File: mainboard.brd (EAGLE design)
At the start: 90.2 x 95.9 mm, 8 parts, among them IC1 FT232RLSSOP, U1 ATMEGA2560AU, U2 ITG-3200

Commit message: Initial commit of power board
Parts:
- removed IC1: FT232RLSSOP, SparkFun:SSOP28DB
- removed U$1: RFM23BP, RFM23BP:RFM23BP
- added C1, C10, C2, C3, C5, C6, C7, C8, C9: 0.1uF, SparkFun:0603-CAP
- added C4: 0.1uF, SparkFun:0402-CAP
- added JP1, JP2: USB-SMD-NS, SparkFun-Connectors:USB-MINIB-NOSTOP
- added LED2: yellow, SparkFun:LED-0603
- added R1, R4, R5: 10k, SparkFun:0603-RES
- added R3: 10k, SparkFun:0402-RES
- added R7: 470, SparkFun:0402-RES
- added SMA1: BU-SMA-V, con-coax:BU-SMA-V
- added U5: ITG-3200, SparkFun-Sensors:QFN-24
- added U6: (no value), SparkFun-DigitalIC:TSSOP14
- added U7: ATMEGA328P, SparkFun:TQFP32-08
- added U8: FT232RLSSOP, SparkFun:SSOP28DB
- added Y1: RESONATORSMD, SparkFun:RESONATOR-SMD
- added Y2: 16MHZ, SparkFun-FreqCtrl:RESONATOR-SMD
- U1: device SparkFun-DigitalIC:TQFP100 -> SparkFun:TQFP100
- U2: value ITG-3200 -> FT232RLSSOP; device SparkFun-Sensors:QFN-24 -> SparkFun:SSOP28DB
- U3: value (none) -> RFM23BP; device SparkFun-DigitalIC:TSSOP14 -> RFM23BP:RFM23BP
- moved U2 46.1 mm to (66.2, 61.6)
- moved U3 19.3 mm to (29.7, 20.7)
- moved U1 5.10 mm to (42.3, 40.3)
- renumbered U$2 to U4
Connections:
- removed net AVCC: U1.100
- removed net GND1: U$1.GND1, U1.32
- removed net GND2: U$1.GND2, U1.62
- removed net GND3: U$1.GND3, U1.81
- removed net VCC1: U1.31
- removed net VCC2: U1.61
- removed net VCC3: U1.80
- new net 3.3V: C6.1, C7.1, C8.1, R3.2, R4.2, R5.2, U1.10, U1.100, U1.31, U1.61, U1.80, U6.1
- new net 5V: C2.1, C3.1, C9.1, R1.2, U3.VCC, U6.14, U7.18, U7.4, U7.6
- new net A0: U1.97
- new net A1: U1.96
- new net A10: U1.87
- new net A11: U1.86
- new net A12: U1.85
- new net A13: U1.84
- new net A14: U1.83
- new net A15: U1.82
- new net A2: U1.95
- new net A3: U1.94
- new net A4: U1.93
- new net A5: U1.92
- new net A6: U1.91
- new net A7: U1.90
- new net A8: U1.89
- new net A9: U1.88
- new net AREF: C5.1, U1.98
- new net DTR: C4.1
- new net DTR2: C1.1
- new net MISO2: U3.SDO, U7.16
- new net MOSI2: U3.SDI, U7.15
- new net N$1: SMA1.1, U3.ANT
- new net N$2: U7.7, Y2.1
- new net N$3: LED2.A, R7.1
- new net N$4: C10.1, U7.20
- new net N$5: U7.8, Y2.3
- new net N$73: U1.33, Y1.1
- new net N$74: U1.34, Y1.3
- new net PA0: U1.78
- new net PA1: U1.77
- new net PA2: U1.76
- new net PA3: U1.75
- new net PA4: U1.74
- new net PA5: U1.73
- new net PA6: U1.72
- new net PA7: U1.71
- new net PB0: U1.19
- new net PB1: U1.20
- new net PB2: U1.21
- new net PB3: U1.22
- new net PB4: U1.23
- new net PB5: U1.24
- new net PB6: U1.25
- new net PB7: R7.2, U1.26
- new net PC0: U1.53
- new net PC1: U1.54
- new net PC2: U1.55
- new net PC3: U1.56
- new net PC4: U1.57
- new net PC5: U1.58
- new net PC6: U1.59
- new net PC7: U1.60
- new net PD7: U1.50
- new net PE3: U1.5
- new net PE4: U1.6
- new net PE5: U1.7
- new net PG0: U1.51
- new net PG1: U1.52
- new net PG2: U1.70
- new net PG5: U1.1
- new net PH3: U1.15
- new net PH4: U1.16
- new net PH5: U1.17
- new net PH6: U1.18
- new net PL0: U1.35
- new net PL1: U1.36
- new net PL2: U1.37
- new net PL3: U1.38
- new net PL4: U1.39
- new net PL5: U1.40
- new net PL6: U1.41
- new net PL7: U1.42
- new net RESET: C4.2, R3.1, U1.30
- new net RESET2: C1.2, R1.1, U7.29
- new net RX0: U1.2
- new net RX1: U1.45
- new net RX2: U1.12
- new net RX3: U1.63
- new net SCK2: U3.SCK, U7.17
- new net SCL: R5.1, U1.43
- new net SDA: R4.1, U1.44
- new net TX0: U1.3
- new net TX1: U1.46
- new net TX2: U1.13
- new net TX3: U1.64
- net AGND: now also U2.25, U8.25; no longer IC1.25, U1.99
- net GND: now also C10.2, C2.2, C3.2, C5.2, C6.2, C7.2, C8.2, C9.2, LED2.C, SMA1.2, SMA1.3, SMA1.4, SMA1.5, U1.32, U1.62, U1.81, U1.99, U3.GND1, U3.GND2, U3.GND3, U6.7, U7.21, U7.3, U7.5, Y1.2, Y2.2
- net GND18: now also U2.18, U8.18; no longer IC1.18
- net GND21: now also U2.21, U8.21; no longer IC1.21
- net GND7: now also U2.7, U8.7; no longer IC1.7
- net VCC: now also U2.20, U8.20; no longer IC1.20, U$1.VCC, U1.10
- net VCCIO: now also U2.4, U8.4; no longer IC1.4

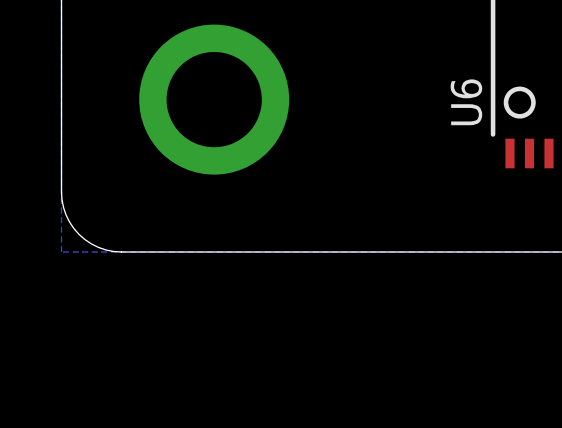
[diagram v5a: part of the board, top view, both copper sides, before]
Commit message: Added RTC
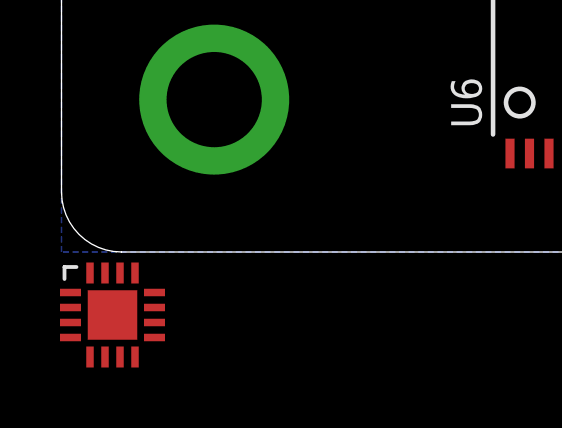
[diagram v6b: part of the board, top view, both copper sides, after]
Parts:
- added U$1: AB0805, AB0805:QFN16
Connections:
- new net VBACKUP: H1.42
- new net VBATT: H2.45, H2.46
- net 3.3V: now also H2.27, H2.28, U$1.VCC
- net 5V: now also H2.25, H2.26
- net GND: now also H2.29, H2.30, H2.31, H2.32, U$1.GND, U$1.GNDPAD
- net SCL: now also H1.43
- net SDA: now also H1.41
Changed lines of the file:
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@@
 <element name="U8" library="SparkFun" package="SSOP28DB" value="FT232RLSSOP" x="59" y="48.7"/>
 <element name="JP2" library="SparkFun-Connectors" package="USB-MINIB-NOSTOP" value="USB-SMD-NS" x="70.5" y="41.9" rot="R180"/>
+<element name="U$1" library="AB0805" package="QFN16" value="AB0805" x="1.7" y="-2.1"/>
 </elements>
 <signals>
@@
 <contactref element="Y2" pad="2"/>
 <contactref element="U6" pad="7"/>
+<contactref element="H2" pad="29"/>
+<contactref element="H2" pad="31"/>
+<contactref element="H2" pad="30"/>
+<contactref element="H2" pad="32"/>
+<contactref element="U$1" pad="GND"/>
+<contactref element="U$1" pad="GNDPAD"/>
+<wire x1="52.07" y1="90.81" x2="82.55" y2="90.805" width="0" layer="19" extent="1-1"/>
+<wire x1="52.07" y1="88.27" x2="52.07" y2="90.81" width="0" layer="19" extent="1-1"/>
+<wire x1="49.53" y1="90.81" x2="52.07" y2="90.81" width="0" layer="19" extent="1-1"/>
+<wire x1="49.53" y1="88.27" x2="52.07" y2="88.27" width="0" layer="19" extent="1-1"/>
+<wire x1="50.65" y1="74.6" x2="49.53" y2="88.27" width="0" layer="19" extent="1-1"/>
 <wire x1="47.55" y1="74.6" x2="50.65" y2="74.6" width="0" layer="19" extent="1-1"/>
 <wire x1="44.45" y1="74.6" x2="47.55" y2="74.6" width="0" layer="19" extent="1-1"/>
@@
 <wire x1="2.4074" y1="30" x2="2.4074" y2="31.6" width="0" layer="19" extent="1-1"/>
 <wire x1="57.8501" y1="29.1499" x2="50.3" y2="39.8" width="0" layer="19" extent="1-1"/>
-<wire x1="13.8" y1="13.2" x2="5.09" y2="5.08" width="0" layer="19" extent="1-1"/>
+<wire x1="62.9499" y1="29.1499" x2="57.8501" y2="29.1499" width="0" layer="19" extent="1-1"/>
+<wire x1="62.9499" y1="24.0501" x2="62.9499" y2="29.1499" width="0" layer="19" extent="1-1"/>
+<wire x1="57.8501" y1="24.0501" x2="57.8501" y2="29.1499" width="0" layer="19" extent="1-1"/>
+<wire x1="13.8" y1="13.2" x2="13.8" y2="27.2" width="0" layer="19" extent="1-1"/>
 <wire x1="18.85" y1="3.2822" x2="13.8" y2="13.2" width="0" layer="19" extent="1-1"/>
+<wire x1="5.09" y1="5.08" x2="13.8" y2="13.2" width="0" layer="19" extent="1-1"/>
+<wire x1="1.7" y1="-2.1" x2="5.09" y2="5.08" width="0" layer="19" extent="1-1"/>
+<wire x1="3.1" y1="-2.85" x2="1.7" y2="-2.1" width="0" layer="19" extent="1-1"/>
 <wire x1="46.6" y1="15.2" x2="57.8501" y2="24.0501" width="0" layer="19" extent="1-1"/>
+<wire x1="85.09" y1="5.08" x2="62.9499" y2="24.0501" width="0" layer="19" extent="1-1"/>
+<wire x1="8.89" y1="90.805" x2="41.35" y2="74.6" width="0" layer="19" extent="1-1"/>
 </signal>
 <signal name="AGND">
@@
 <contactref element="U1" pad="43"/>
 <contactref element="R5" pad="1"/>
+<contactref element="H1" pad="43"/>
+<wire x1="36.55" y1="70.7" x2="67.31" y2="83.19" width="0" layer="19" extent="1-1"/>
 <wire x1="44.8" y1="32.3" x2="36.55" y2="70.7" width="0" layer="19" extent="1-1"/>
 </signal>
@@
 <contactref element="R4" pad="1"/>
 <contactref element="U1" pad="44"/>
+<contactref element="H1" pad="41"/>
+<wire x1="33.45" y1="70.7" x2="64.77" y2="83.19" width="0" layer="19" extent="1-1"/>
 <wire x1="45.3" y1="32.3" x2="33.45" y2="70.7" width="0" layer="19" extent="1-1"/>
 </signal>
@@
 <contactref element="R5" pad="2"/>
 <contactref element="U6" pad="1"/>
-<wire x1="45.85" y1="74.6" x2="48.95" y2="74.6" width="0" layer="19" extent="1-1"/>
+<contactref element="H2" pad="27"/>
+<contactref element="H2" pad="28"/>
+<contactref element="U$1" pad="VCC"/>
+<wire x1="46.99" y1="88.27" x2="46.99" y2="90.81" width="0" layer="19" extent="1-1"/>
+<wire x1="45.85" y1="74.6" x2="46.99" y2="88.27" width="0" layer="19" extent="1-1"/>
+<wire x1="48.95" y1="74.6" x2="45.85" y2="74.6" width="0" layer="19" extent="1-1"/>
 <wire x1="42.75" y1="74.6" x2="45.85" y2="74.6" width="0" layer="19" extent="1-1"/>
 <wire x1="38.25" y1="70.7" x2="42.75" y2="74.6" width="0" layer="19" extent="1-1"/>
@@
 <wire x1="38.8" y1="32.3" x2="34.3" y2="41.8" width="0" layer="19" extent="1-1"/>
 <wire x1="14.95" y1="3.2822" x2="38.8" y2="32.3" width="0" layer="19" extent="1-1"/>
+<wire x1="2.45" y1="-0.7" x2="14.95" y2="3.2822" width="0" layer="19" extent="1-1"/>
 </signal>
 <signal name="DTR">
@@
 <contactref element="C3" pad="1"/>
 <contactref element="U6" pad="14"/>
+<contactref element="H2" pad="25"/>
+<contactref element="H2" pad="26"/>
+<wire x1="44.45" y1="88.27" x2="44.45" y2="90.81" width="0" layer="19" extent="1-1"/>
+<wire x1="32.05" y1="52.4" x2="44.45" y2="88.27" width="0" layer="19" extent="1-1"/>
 <wire x1="22.05" y1="49.4" x2="32.05" y2="52.4" width="0" layer="19" extent="1-1"/>
 <wire x1="22.05" y1="46.4" x2="22.05" y2="49.4" width="0" layer="19" extent="1-1"/>
@@
 <wire x1="13.8" y1="21.2" x2="10.9926" y2="27.6" width="0" layer="19" extent="1-1"/>
 </signal>
+<signal name="VBATT">
+<contactref element="H2" pad="45"/>
+<contactref element="H2" pad="46"/>
+<wire x1="69.85" y1="88.27" x2="69.85" y2="90.81" width="0" layer="19" extent="1-1"/>
+</signal>
+<signal name="VBACKUP">
+<contactref element="H1" pad="42"/>
+</signal>
 </signals>

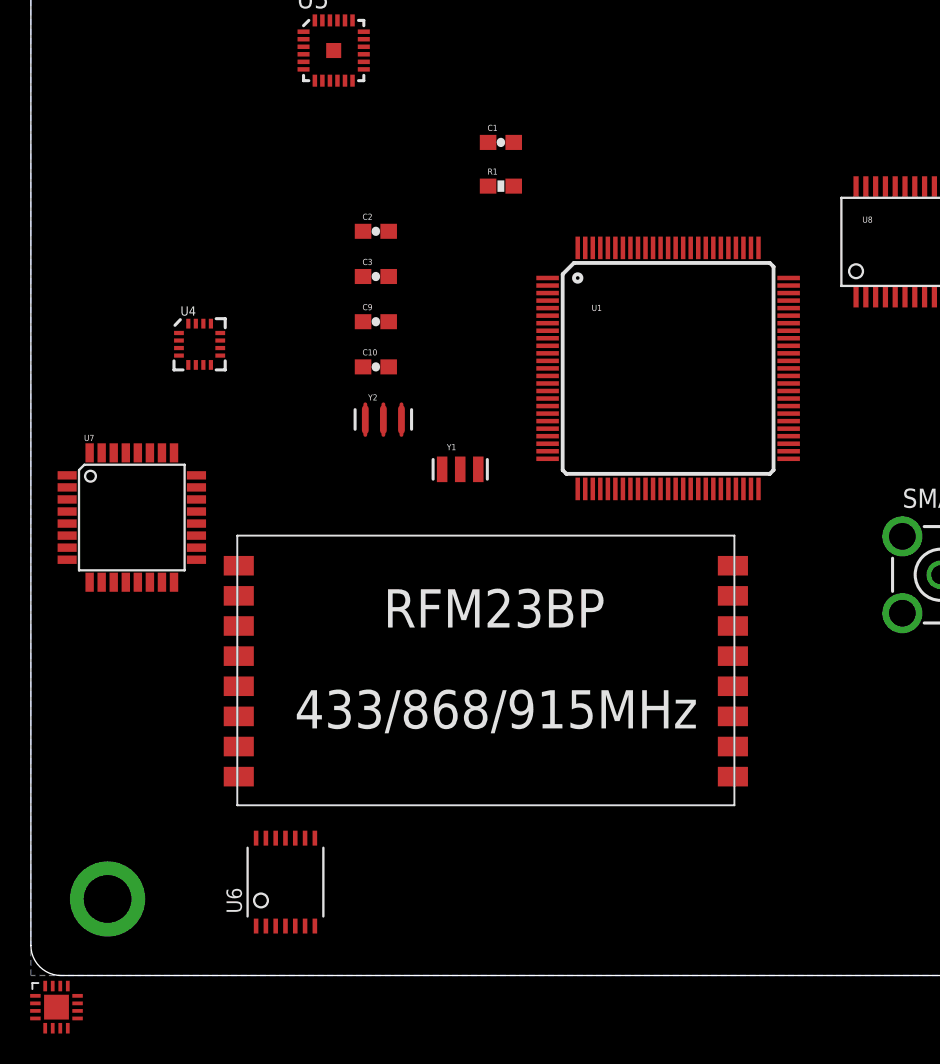
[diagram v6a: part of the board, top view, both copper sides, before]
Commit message: Added Micrel voltage supervisors
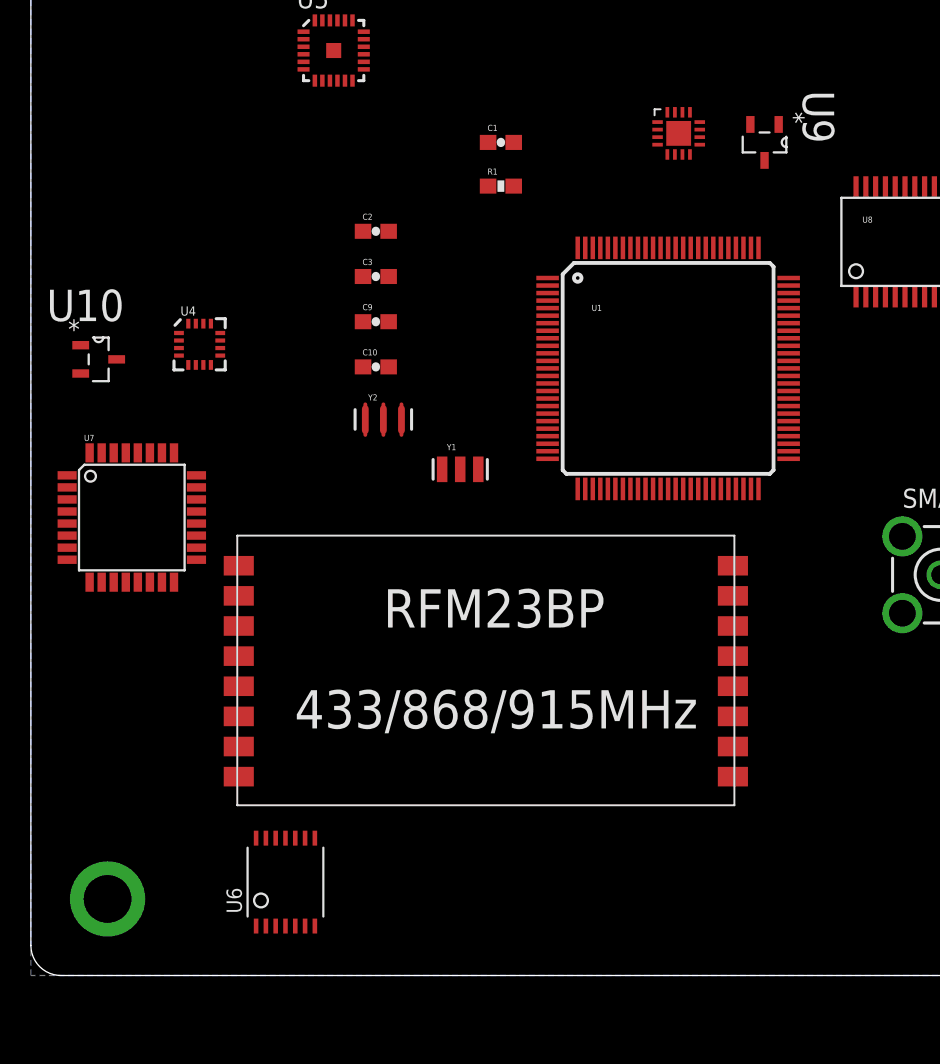
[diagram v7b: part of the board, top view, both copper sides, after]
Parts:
- added U10: MIC803-46D3VM3TR, Micrel:SOT95P232X110-3N
- added U9: MIC803-31D3VM3TR, Micrel:SOT95P232X110-3N
- moved U$1 71.2 mm to (43.0, 55.9)
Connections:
- net VCC: now also U10.3, U9.3
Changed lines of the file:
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@@
 <element name="U8" library="SparkFun" package="SSOP28DB" value="FT232RLSSOP" x="59" y="48.7"/>
 <element name="JP2" library="SparkFun-Connectors" package="USB-MINIB-NOSTOP" value="USB-SMD-NS" x="70.5" y="41.9" rot="R180"/>
-<element name="U$1" library="AB0805" package="QFN16" value="AB0805" x="1.7" y="-2.1"/>
+<element name="U$1" library="AB0805" package="QFN16" value="AB0805" x="43" y="55.9"/>
+<element name="U9" library="Micrel" package="SOT95P232X110-3N" value="MIC803-31D3VM3TR" x="48.7" y="55.3" rot="R270">
+<attribute name="PACKAGE" value="SOT-23-3" x="48.7" y="55.3" size="1.778" layer="27" rot="R270" display="off"/>
+<attribute name="OC_NEWARK" value="58T4953" x="48.7" y="55.3" size="1.778" layer="27" rot="R270" display="off"/>
+<attribute name="MPN" value="MIC803-31D3VM3TR" x="48.7" y="55.3" size="1.778" layer="27" rot="R270" display="off"/>
+<attribute name="SUPPLIER" value="MICREL SEMICONDUCTOR" x="48.7" y="55.3" size="1.778" layer="27" rot="R270" display="off"/>
+<attribute name="OC_FARNELL" value="1924772" x="48.7" y="55.3" size="1.778" layer="27" rot="R270" display="off"/>
+</element>
+<element name="U10" library="Micrel" package="SOT95P232X110-3N" value="MIC803-46D3VM3TR" x="4.5" y="40.9">
+<attribute name="PACKAGE" value="SOT-23-3" x="4.5" y="40.9" size="1.778" layer="27" display="off"/>
+<attribute name="OC_NEWARK" value="58T4965" x="4.5" y="40.9" size="1.778" layer="27" display="off"/>
+<attribute name="MPN" value="MIC803-46D3VM3TR" x="4.5" y="40.9" size="1.778" layer="27" display="off"/>
+<attribute name="SUPPLIER" value="MICREL SEMICONDUCTOR" x="4.5" y="40.9" size="1.778" layer="27" display="off"/>
+<attribute name="OC_FARNELL" value="1924785" x="4.5" y="40.9" size="1.778" layer="27" display="off"/>
+</element>
 </elements>
 <signals>
@@
 <wire x1="18.85" y1="3.2822" x2="13.8" y2="13.2" width="0" layer="19" extent="1-1"/>
 <wire x1="5.09" y1="5.08" x2="13.8" y2="13.2" width="0" layer="19" extent="1-1"/>
-<wire x1="1.7" y1="-2.1" x2="5.09" y2="5.08" width="0" layer="19" extent="1-1"/>
-<wire x1="3.1" y1="-2.85" x2="1.7" y2="-2.1" width="0" layer="19" extent="1-1"/>
+<wire x1="43" y1="55.9" x2="5.09" y2="5.08" width="0" layer="19" extent="1-1"/>
+<wire x1="44.4" y1="55.15" x2="43" y2="55.9" width="0" layer="19" extent="1-1"/>
 <wire x1="46.6" y1="15.2" x2="57.8501" y2="24.0501" width="0" layer="19" extent="1-1"/>
 <wire x1="85.09" y1="5.08" x2="62.9499" y2="24.0501" width="0" layer="19" extent="1-1"/>
@@
 <contactref element="U2" pad="20"/>
 <contactref element="U8" pad="20"/>
+<contactref element="U9" pad="3"/>
+<contactref element="U10" pad="3"/>
 <wire x1="59.975" y1="52.356" x2="67.175" y2="65.256" width="0" layer="19" extent="1-1"/>
+<wire x1="48.7" y1="54.1062" x2="59.975" y2="52.356" width="0" layer="19" extent="1-1"/>
+<wire x1="5.6938" y1="40.9" x2="48.7" y2="54.1062" width="0" layer="19" extent="1-1"/>
 </signal>
 <signal name="GND7">
@@
 <wire x1="38.8" y1="32.3" x2="34.3" y2="41.8" width="0" layer="19" extent="1-1"/>
 <wire x1="14.95" y1="3.2822" x2="38.8" y2="32.3" width="0" layer="19" extent="1-1"/>
-<wire x1="2.45" y1="-0.7" x2="14.95" y2="3.2822" width="0" layer="19" extent="1-1"/>
+<wire x1="43.75" y1="57.3" x2="14.95" y2="3.2822" width="0" layer="19" extent="1-1"/>
 </signal>
 <signal name="DTR">

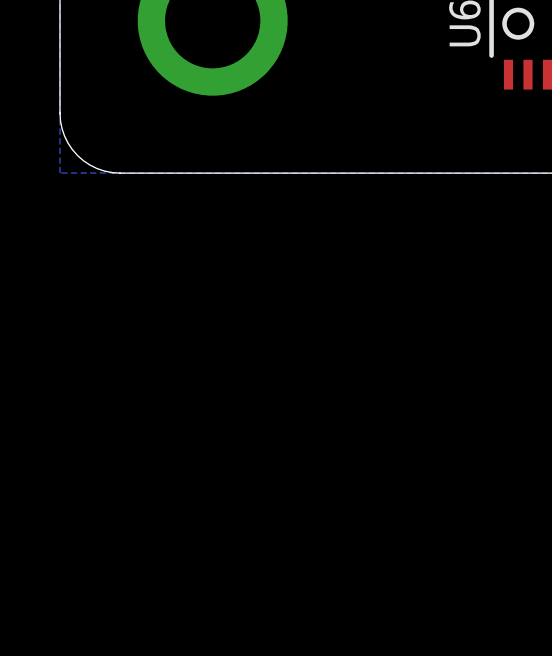
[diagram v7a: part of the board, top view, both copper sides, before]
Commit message: Added new side solar panel
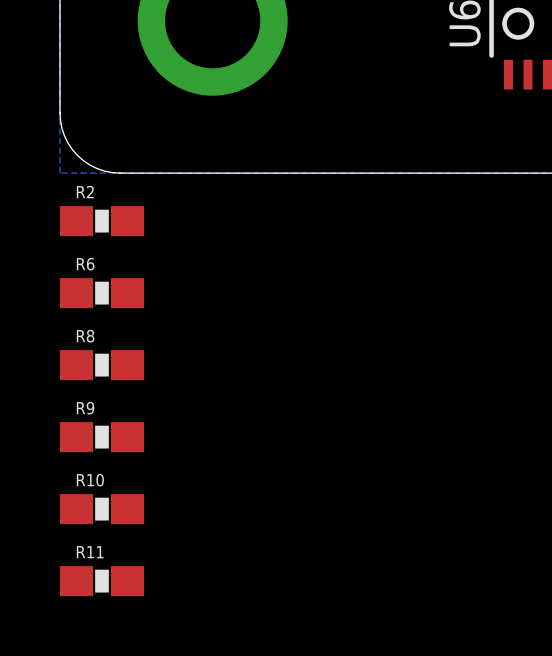
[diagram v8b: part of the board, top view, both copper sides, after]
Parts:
- added R10, R11: 10k, SparkFun-Passives:0603-RES
- added R2: 1.25R, SparkFun-Passives:0603-RES
- added R6: 680R, SparkFun-Passives:0603-RES
- added R8: 0.75R, SparkFun-Passives:0603-RES
- added R9: 470R, SparkFun-Passives:0603-RES
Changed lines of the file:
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@@
 <attribute name="OC_FARNELL" value="1924785" x="4.5" y="40.9" size="1.778" layer="27" display="off"/>
 </element>
+<element name="R2" library="SparkFun-Passives" package="0603-RES" value="1.25R" x="1.4" y="-1.6"/>
+<element name="R6" library="SparkFun-Passives" package="0603-RES" value="680R" x="1.4" y="-4"/>
+<element name="R8" library="SparkFun-Passives" package="0603-RES" value="0.75R" x="1.4" y="-6.4"/>
+<element name="R9" library="SparkFun-Passives" package="0603-RES" value="470R" x="1.4" y="-8.8"/>
+<element name="R10" library="SparkFun-Passives" package="0603-RES" value="10k" x="1.4" y="-11.2"/>
+<element name="R11" library="SparkFun-Passives" package="0603-RES" value="10k" x="1.4" y="-13.6"/>
 </elements>
 <signals>
@@
 <contactref element="R1" pad="2"/>
 <contactref element="U3" pad="VCC"/>
+<contactref element="U6" pad="14"/>
+<contactref element="H2" pad="25"/>
+<contactref element="H2" pad="26"/>
 <contactref element="U7" pad="18"/>
 <contactref element="C2" pad="1"/>
@@
 <contactref element="U7" pad="4"/>
 <contactref element="C3" pad="1"/>
-<contactref element="U6" pad="14"/>
-<contactref element="H2" pad="25"/>
-<contactref element="H2" pad="26"/>
 <wire x1="44.45" y1="88.27" x2="44.45" y2="90.81" width="0" layer="19" extent="1-1"/>
 <wire x1="32.05" y1="52.4" x2="44.45" y2="88.27" width="0" layer="19" extent="1-1"/>
